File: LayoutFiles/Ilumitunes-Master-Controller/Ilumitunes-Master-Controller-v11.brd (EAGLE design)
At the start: 59.7 x 53.3 mm, 13 parts, among them U1 ARDUINO_SHIELD

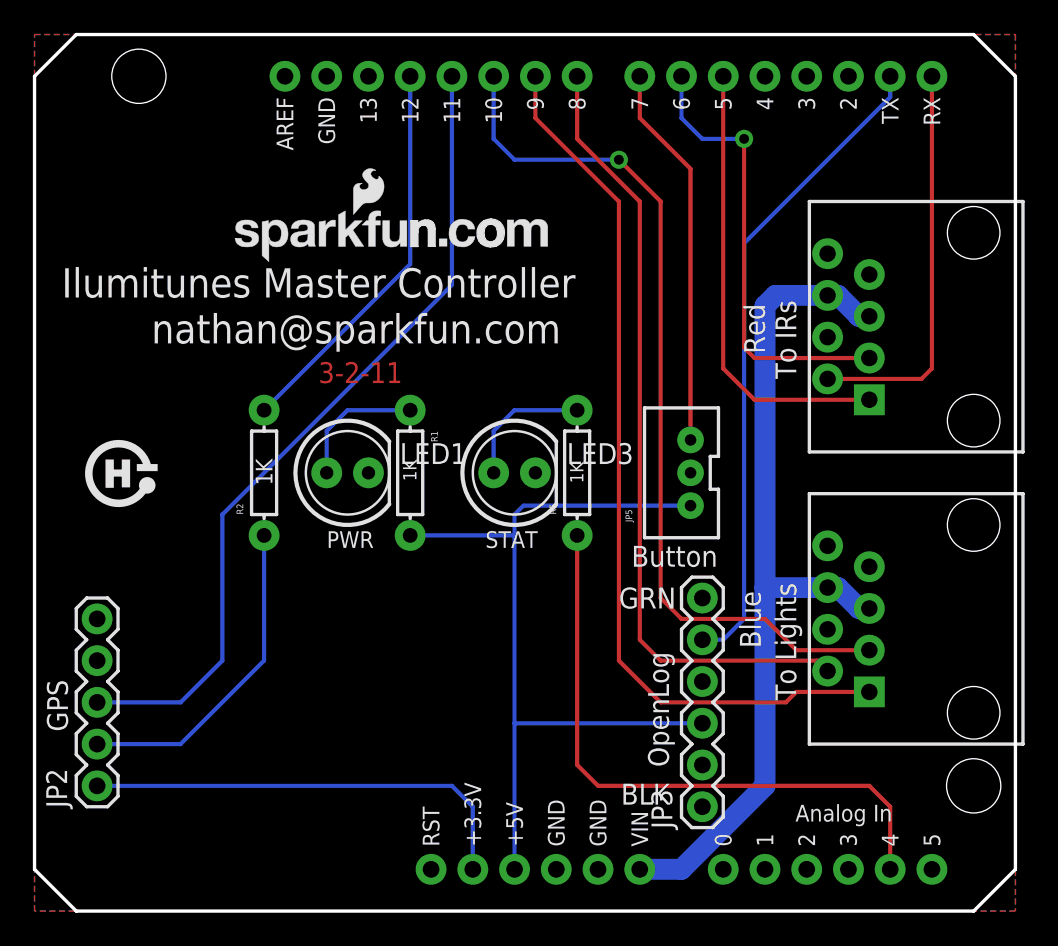
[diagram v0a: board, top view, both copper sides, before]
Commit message: Added more PTC and decoupling to string controller at breakout.
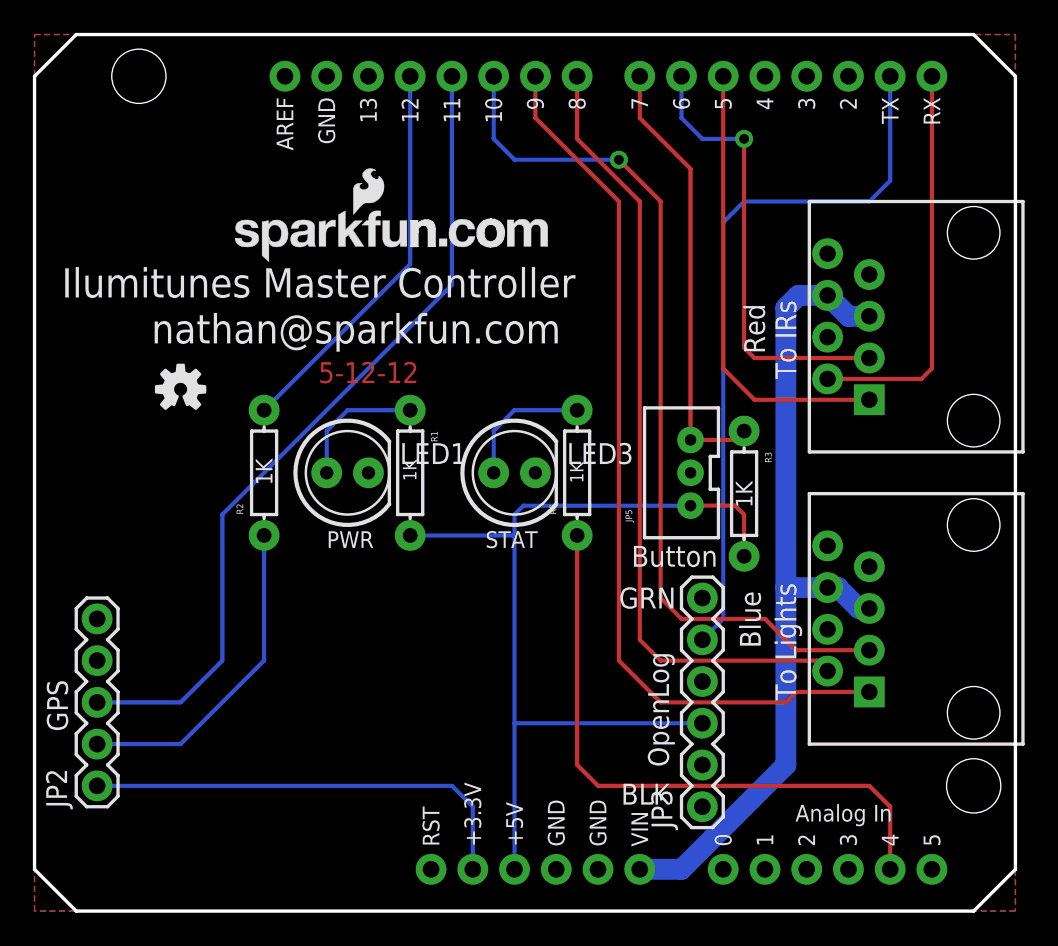
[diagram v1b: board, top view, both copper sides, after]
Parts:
- added R3: 1K, SparkFun-Passives:AXIAL-0.3
- added U$3: OSHW-LOGOS, SparkFun-Aesthetics:OSHW-LOGO-S
- U$2: value OSHW-LOGO -> CREATIVE_COMMONS; device SparkFun:OSHW-LOGO -> SparkFun-Aesthetics:CREATIVE_COMMONS
- moved U$2 44.5 mm to (6.35, -17.8)
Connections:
- net BUTTON: now also R3.P$1
- net VCC: now also R3.P$2
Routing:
- net VCC: track 50.3 -> 56.3 mm
- net LOGGER-RX: track 39.8 -> 43.5 mm
- net BUTTON: track 23.4 -> 26.9 mm
- net VIN: track 52.9 -> 51.0 mm
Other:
- board text added: "5-12-12"
- board text removed: "3-2-11"
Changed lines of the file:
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@@
 <layer number="121" name="_tsilk" color="7" fill="1" visible="no" active="yes"/>
 <layer number="122" name="_bsilk" color="7" fill="1" visible="no" active="yes"/>
+<layer number="125" name="_tNames" color="7" fill="1" visible="no" active="yes"/>
 <layer number="144" name="Drill_legend" color="7" fill="1" visible="no" active="yes"/>
 <layer number="151" name="HeatSink" color="7" fill="1" visible="no" active="yes"/>
@@
 <layer number="215" name="215bmp" color="7" fill="1" visible="no" active="yes"/>
 <layer number="216" name="216bmp" color="7" fill="1" visible="no" active="yes"/>
+<layer number="217" name="217bmp" color="18" fill="1" visible="no" active="no"/>
+<layer number="218" name="218bmp" color="19" fill="1" visible="no" active="no"/>
+<layer number="219" name="219bmp" color="20" fill="1" visible="no" active="no"/>
+<layer number="220" name="220bmp" color="21" fill="1" visible="no" active="no"/>
+<layer number="221" name="221bmp" color="22" fill="1" visible="no" active="no"/>
+<layer number="222" name="222bmp" color="23" fill="1" visible="no" active="no"/>
+<layer number="223" name="223bmp" color="24" fill="1" visible="no" active="no"/>
+<layer number="224" name="224bmp" color="25" fill="1" visible="no" active="no"/>
 <layer number="250" name="Descript" color="7" fill="1" visible="no" active="no"/>
 <layer number="251" name="SMDround" color="7" fill="1" visible="no" active="no"/>
@@
 <wire x1="-2.54" y1="26.67" x2="71.12" y2="26.67" width="0.254" layer="51"/>
 <text x="1.651" y="37.338" size="1.778" layer="21" ratio="15">Ilumitunes Master Controller</text>
-<text x="17.272" y="32.131" size="1.27" layer="1" font="vector" ratio="25">3-2-11</text>
+<text x="17.272" y="32.131" size="1.27" layer="1" font="vector" ratio="25">5-12-12</text>
 <text x="27.432" y="22.098" size="1.016" layer="21" font="vector" ratio="15">STAT</text>
 <text x="17.78" y="22.098" size="1.016" layer="21" font="vector" ratio="15">PWR</text>
@@
 <element name="JP9" library="SparkFun" package="RJ45-8" value="Light Controller" x="57.15" y="17.78" rot="R90"/>
 <element name="JP5" library="SparkFun" package="JST-3-PTH-VERT" value="" x="39.37" y="26.67" rot="R90"/>
-<element name="U$2" library="SparkFun" package="OSHW-LOGO" value="OSHW-LOGO" x="5.08" y="26.67"/>
 <element name="JP2" library="SparkFun" package="1X05" value="GPS" x="3.81" y="7.62" rot="R90"/>
 <element name="JP3" library="SparkFun" package="1X06" value="Datalogger" x="40.64" y="6.35" rot="R90"/>
@@
 <attribute name="NAME" x="12.7" y="24.13" size="0.4064" layer="25" font="vector" rot="R90"/>
 <attribute name="VALUE" x="14.478" y="25.908" size="1.016" layer="21" font="vector" ratio="15" rot="R90"/>
+</element>
+<element name="U$3" library="SparkFun-Aesthetics" package="OSHW-LOGO-S" value="OSHW-LOGOS" x="8.89" y="31.75"/>
+<element name="U$2" library="SparkFun-Aesthetics" package="CREATIVE_COMMONS" value="CREATIVE_COMMONS" x="6.35" y="-17.78"/>
+<element name="R3" library="SparkFun-Passives" package="AXIAL-0.3" value="1K" x="43.18" y="25.4" smashed="yes" rot="R270">
+<attribute name="NAME" x="44.45" y="27.94" size="0.4064" layer="25" font="vector" rot="R270"/>
+<attribute name="VALUE" x="42.672" y="26.162" size="1.016" layer="21" font="vector" ratio="15" rot="R270"/>
 </element>
 </elements>
@@
 <wire x1="29.21" y1="22.86" x2="22.86" y2="22.86" width="0.254" layer="16"/>
 <wire x1="29.21" y1="11.43" x2="40.64" y2="11.43" width="0.254" layer="16"/>
+<contactref element="R3" pad="P$2"/>
+<wire x1="39.92" y1="24.67" x2="42.64" y2="24.67" width="0.254" layer="1"/>
+<wire x1="42.64" y1="24.67" x2="43.18" y2="24.13" width="0.254" layer="1"/>
+<wire x1="43.18" y1="24.13" x2="43.18" y2="21.59" width="0.254" layer="1"/>
 </signal>
 <signal name="N$1">
@@
 </signal>
 <signal name="VIN">
+<contactref element="U1" pad="VIN"/>
+<wire x1="36.83" y1="2.54" x2="39.37" y2="2.54" width="1.27" layer="16"/>
+<wire x1="39.37" y1="2.54" x2="45.72" y2="8.89" width="1.27" layer="16"/>
 <contactref element="JP11" pad="5"/>
 <contactref element="JP11" pad="6"/>
+<contactref element="JP9" pad="6"/>
 <contactref element="JP9" pad="5"/>
-<contactref element="JP9" pad="6"/>
-<contactref element="U1" pad="VIN"/>
-<wire x1="44.45" y1="19.685" x2="44.45" y2="36.83" width="1.27" layer="16"/>
-<wire x1="50.165" y1="36.195" x2="50.8" y2="36.195" width="1.27" layer="16"/>
-<wire x1="48.26" y1="37.465" x2="48.895" y2="37.465" width="1.27" layer="16"/>
-<wire x1="48.895" y1="37.465" x2="50.165" y2="36.195" width="1.27" layer="16"/>
-<wire x1="45.085" y1="37.465" x2="48.26" y2="37.465" width="1.27" layer="16"/>
-<wire x1="44.45" y1="36.83" x2="45.085" y2="37.465" width="1.27" layer="16"/>
-<wire x1="50.165" y1="18.415" x2="50.8" y2="18.415" width="1.27" layer="16"/>
+<wire x1="50.165" y1="18.415" x2="50.927" y2="18.415" width="1.27" layer="16"/>
+<wire x1="50.8" y1="36.195" x2="49.53" y2="36.195" width="1.27" layer="16"/>
+<wire x1="49.53" y1="36.195" x2="48.26" y2="37.465" width="1.27" layer="16"/>
+<wire x1="45.72" y1="8.89" x2="45.72" y2="19.685" width="1.27" layer="16"/>
+<wire x1="45.72" y1="19.685" x2="45.72" y2="36.703" width="1.27" layer="16"/>
+<wire x1="45.72" y1="36.703" x2="46.482" y2="37.465" width="1.27" layer="16"/>
+<wire x1="46.482" y1="37.465" x2="48.26" y2="37.465" width="1.27" layer="16"/>
+<wire x1="48.26" y1="19.685" x2="45.72" y2="19.685" width="1.27" layer="16"/>
 <wire x1="48.26" y1="19.685" x2="48.895" y2="19.685" width="1.27" layer="16"/>
 <wire x1="48.895" y1="19.685" x2="50.165" y2="18.415" width="1.27" layer="16"/>
-<wire x1="44.45" y1="19.685" x2="48.26" y2="19.685" width="1.27" layer="16"/>
-<wire x1="36.83" y1="2.54" x2="39.37" y2="2.54" width="1.27" layer="16"/>
-<wire x1="39.37" y1="2.54" x2="44.45" y2="7.62" width="1.27" layer="16"/>
-<wire x1="44.45" y1="7.62" x2="44.45" y2="19.685" width="1.27" layer="16"/>
+<wire x1="50.927" y1="18.415" x2="50.8" y2="18.415" width="0" layer="19" extent="16-16"/>
 </signal>
 <signal name="DETECTOR-TX">
@@
 <wire x1="39.92" y1="45.17" x2="36.83" y2="48.26" width="0.254" layer="1"/>
 <wire x1="36.83" y1="48.26" x2="36.83" y2="50.8" width="0.254" layer="1"/>
+<contactref element="R3" pad="P$1"/>
+<wire x1="39.92" y1="28.67" x2="42.64" y2="28.67" width="0.254" layer="1"/>
+<wire x1="42.64" y1="28.67" x2="43.18" y2="29.21" width="0.254" layer="1"/>
 </signal>
 <signal name="DETECTOR-RX">
@@
 <contactref element="U1" pad="TX"/>
 <contactref element="JP3" pad="5"/>
-<wire x1="40.64" y1="16.51" x2="41.91" y2="16.51" width="0.254" layer="16"/>
-<wire x1="41.91" y1="16.51" x2="43.18" y2="17.78" width="0.254" layer="16"/>
-<wire x1="43.18" y1="17.78" x2="43.18" y2="40.64" width="0.254" layer="16"/>
-<wire x1="43.18" y1="40.64" x2="52.07" y2="49.53" width="0.254" layer="16"/>
-<wire x1="52.07" y1="49.53" x2="52.07" y2="50.8" width="0.254" layer="16"/>
+<wire x1="52.07" y1="50.8" x2="52.07" y2="44.45" width="0.254" layer="16"/>
+<wire x1="52.07" y1="44.45" x2="50.8" y2="43.18" width="0.254" layer="16"/>
+<wire x1="50.8" y1="43.18" x2="43.18" y2="43.18" width="0.254" layer="16"/>
+<wire x1="43.18" y1="43.18" x2="41.91" y2="41.91" width="0.254" layer="16"/>
+<wire x1="41.91" y1="41.91" x2="41.91" y2="17.78" width="0.254" layer="16"/>
+<wire x1="41.91" y1="17.78" x2="40.64" y2="16.51" width="0.254" layer="16"/>
 </signal>
 <signal name="GPS-RX">
@@
 <wire x1="26.67" y1="6.35" x2="26.67" y2="2.54" width="0.254" layer="16"/>
 </signal>
+<signal name="N$2">
+</signal>
 </signals>
